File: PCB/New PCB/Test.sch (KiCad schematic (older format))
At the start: 32 parts, among them IC1 REG1117, P1 CONN_2, P2 BATT_CONN, SW1 SWITCH_INV, X1 20 MHz

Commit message: update of new pcb and power supply design
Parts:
- removed ACCELEROMETER1: AIS328DQ, ~, symbol AIS328DQ
- removed C1, C2, C8: C, ~, symbol C
- removed C10, C11: DNI, ~, symbol C
- removed C12: 1uF, ~, symbol C
- removed C13, C3, C6, C7: 0.1 uF, ~, symbol C
- removed C4: 10 nF, ~, symbol C
- removed C5: 470 nF, ~, symbol C
- removed C9: C1 nF, ~, symbol C
- removed CURRENT1: ACS716, symbol ACS716
- removed GYROSCOPE1: A3G4250D, ~, symbol A3G4250D
- removed IC1: REG1117, symbol REG1117
- removed JP1: MOT_ENC, symbol MOT_ENC
- removed JP2: JP, symbol JP
- removed JP3: M05X2PTH, symbol M05X2PTH
- removed JP4: M013X2PTH, symbol M013X2PTH
- removed MOTOR1: LS7366RDIP, symbol LS7366RDIP
- removed P1: CONN_2, symbol CONN_2
- removed P2: BATT_CONN, symbol CONN_2
- removed R1: R, ~, symbol R
- removed R2: 10K, ~, symbol R
- removed R3, R4: DNI, ~, symbol R
- removed R5: 330, ~, symbol R
- removed SW1: SWITCH_INV, ~, symbol SWITCH_INV
- removed X1: 20 MHz, ~, symbol QUARTZCMS4
- added U?: DSPIC33EP512MC806, ~, symbol DSPIC33EP512MC806
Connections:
- net labels removed: +5V, DFLAG, DIO1, DIO2, FAULT_EN, INT1, INT2, INT_1, INT_2, LFLAG, SPI_CLK, SPI_DIN, SPI_DOUT, SPI_SS, VIOUT
- wire segments 166 -> 9
- no-connect marks 36 -> 16
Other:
- note added: "Sensors"
- note added: "XBee Chip"
- moved on the sheet: XBEE1

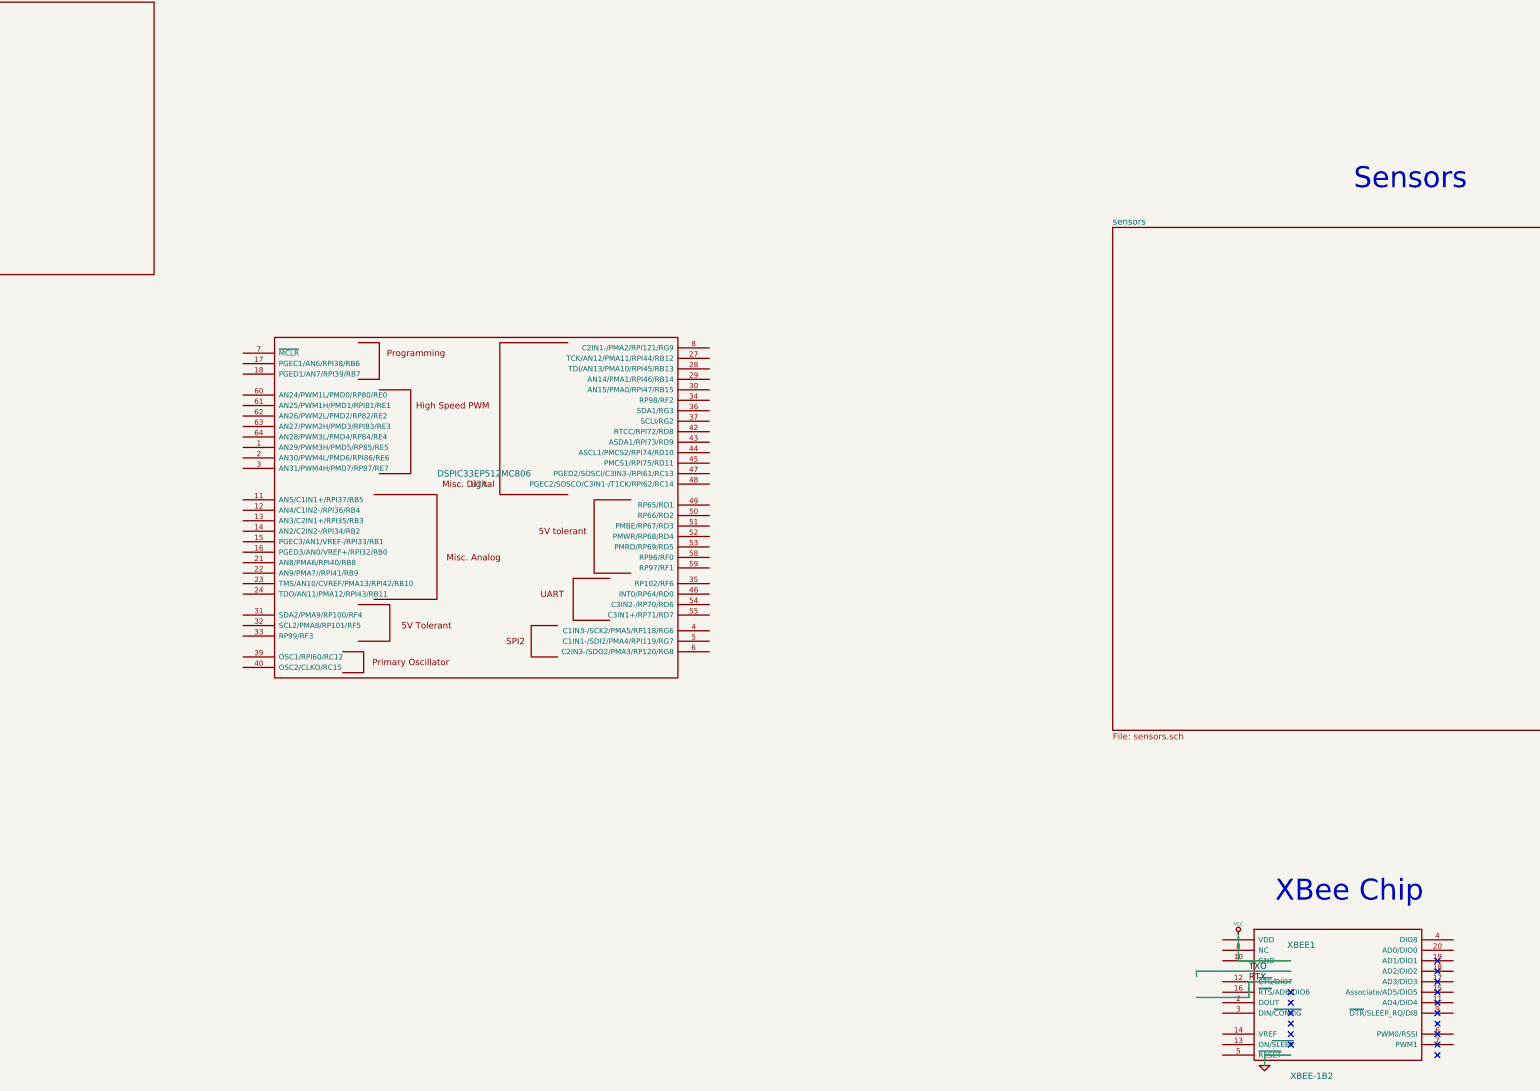
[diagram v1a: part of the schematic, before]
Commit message: Updating Schematic for New PCB
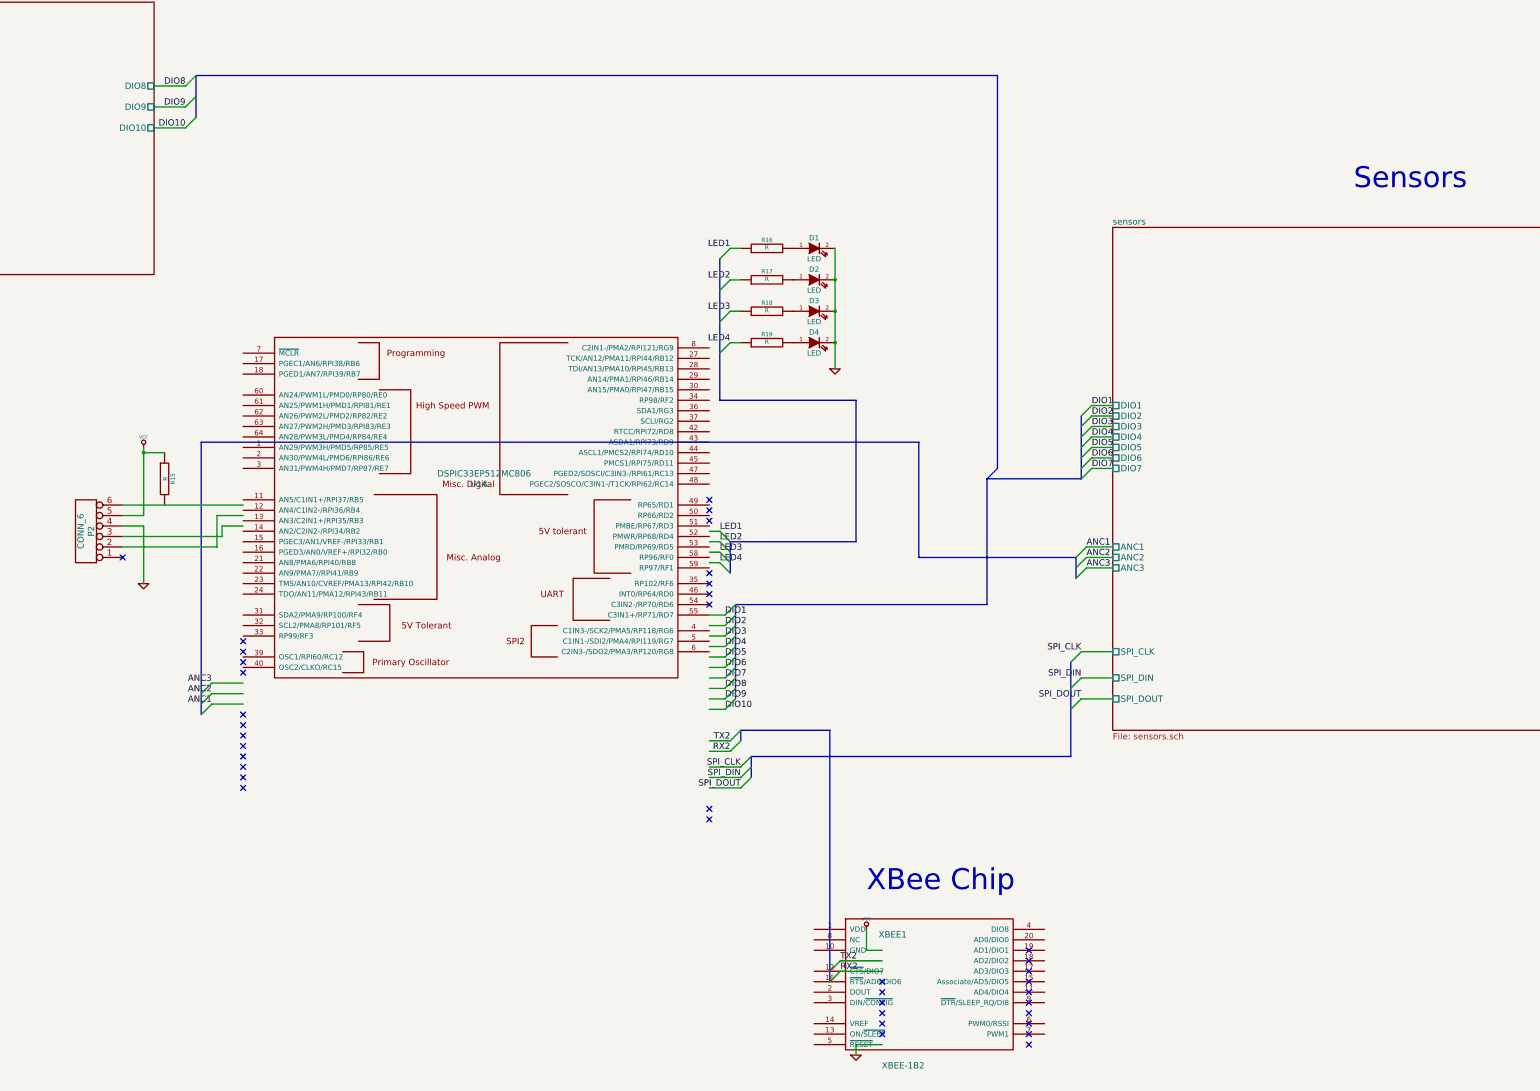
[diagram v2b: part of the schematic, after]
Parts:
- added D1, D2, D3, D4: LED, ~, symbol LED
- added P2: CONN_6, symbol CONN_6
- added R15, R16, R17, R18, R19: R, ~, symbol R
- gave numbers to parts that had none: 1
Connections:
- net labels added: ANC1, ANC2, ANC3, DIO1, DIO10, DIO2, DIO3, DIO4, DIO5, DIO6, DIO7, DIO8, DIO9, LED1, LED2, LED3, LED4, RX2, SPI_CLK, SPI_DIN, SPI_DOUT, TX2
- net labels removed: RTX, TXO
- wire segments 9 -> 61
- no-connect marks 16 -> 38
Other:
- moved on the sheet: XBEE1

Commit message: updated schematic
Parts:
- removed P2: CONN_6, symbol CONN_6
- added CR?: CER_RES, symbol CER_RES
- added JP? (x2): MOT_ENC, symbol MOT_ENC
- added P?: PROG_H, symbol PROG_H
- R15: value R -> 10K
- R16, R17, R18, R19: value R -> 1K
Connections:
- net labels added: +5V, ENC1, ENC2, ENC3, ENC4, ENC5, ENC6
- wire segments 61 -> 69
- no-connect marks 38 -> 29
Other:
- note added: "Power"
- moved on the sheet: D1, D2, D3, D4, R15, R16, R17, R18, R19, U1A, XBEE1

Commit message: more updates
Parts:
- added P?: CONN_2, symbol CONN_2
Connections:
- net labels added: CTS, MagnetControl1, MagnetControl2, MagnetControl[1:2], MotorOut[1:3], Motor_Control[1:6], PWM1H, PWM1L, PWM2H, PWM2L, PWM3H, PWM3L, RTS, RX, SPI_BUS[1:3], TX
- wire segments 69 -> 73
- no-connect marks 29 -> 25
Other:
- note added: "Reset Switch"
- moved on the sheet: XBEE1

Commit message: updated schematic
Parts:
- added D5: LED, ~, symbol LED
- added R2: 1K, ~, symbol R
- added R32: 1M, symbol R
- gave numbers to parts that had none: 5
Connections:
- net labels added: ACCEL1, ACCEL2, ACCEL3, ACCEL[1:3], ANC[1:3], ENCODER1, ENCODER2, ENCODER3, ENCODER4, ENCODER5, ENCODER6, ENC[1:3], GYRO1, GYRO2, GYRO3, GYRO[1:3], LED5, MotorOut[0:2]
- net labels removed: DIO1, DIO10, DIO2, DIO3, DIO4, DIO5, DIO6, DIO7, DIO8, DIO9, ENC4, ENC5, ENC6, MotorOut[1:3]
- wire segments 73 -> 63
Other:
- note added: "NOTE: Global VCC = +3.3V"
- note added: "Need to add the motor hall effect sensors"
- moved on the sheet: D1, D2, D3, D4, R16, R17, R18, R19

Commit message: added notes to schematic
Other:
- note added: "3 on each end of board"
- note added: "6 IR LEDs for Vision group"
- note added: "Add LED"
- note added: "Add decoupling"
- note added: "Change Labels"
- note added: "Mounting Holes as well"
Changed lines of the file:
@@
-EESchema Schematic File Version 2
+EESchema Schematic File Version 2  date 6/2/2013 3:28:30 PM
 LIBS:power
 LIBS:device
@@
 Text Notes 6200 9450 0    60   ~ 0
 Need to add the motor hall effect sensors
+Text Notes 12000 12550 0    60   ~ 0
+Add LED
+Text Notes 8150 13200 0    60   ~ 0
+Change Labels
+Text Notes 10300 14550 0    60   ~ 0
+Add decoupling
+Text Notes 4700 1850 0    157  ~ 0
+6 IR LEDs for Vision group
+Text Notes 5750 2150 0    60   ~ 0
+3 on each end of board
+Text Notes 15500 1750 0    157  ~ 0
+Mounting Holes as well
 $EndSCHEMATC

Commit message: updated schematic and netlist, added flyback diodes
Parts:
- added C53: 0.1uF, symbol C
- added D9: LED, symbol LED
- added P10, P11, P6, P7, P8, P9: CONN_2, symbol CONN_2
- added P12, P13, P14, P15: CONN_1, symbol CONN_1
- added P16: CONN_6, symbol CONN_6
- added R38, R39, R40, R41, R42, R43: 330, symbol R
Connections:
- net labels added: ACCEL0, ACCEL[0..2], ANC0, ANC[0..2], ENC0, ENC[0..2], GYRO0, GYRO[0..2], MagnetControl0, MagnetControl[0..1], MotorControl0, MotorControl1, MotorControl2, MotorControl3, MotorControl4, MotorControl5, MotorControl[0..5], MotorOut[0..2], SPI_BUS0, SPI_BUS1, SPI_BUS2, SPI_BUS[0..2]
- net labels removed: ACCEL3, ACCEL[1:3], ANC3, ANC[1:3], ENC3, ENC[1:3], GYRO3, GYRO[1:3], MagnetControl2, MagnetControl[1:2], MotorOut[0:2], Motor_Control[1:6], PWM1H, PWM1L, PWM2H, PWM2L, PWM3H, PWM3L, RX2, SPI_BUS[1:3], SPI_CLK, SPI_DIN, SPI_DOUT, TX2
- wire segments 63 -> 77
- no-connect marks 25 -> 26
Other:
- note added: "Actuators"
- note added: "Hall effect connector"
- note added: "Mounting Holes"
- note added: "Programming header"
- note added: "Status LED"
- note removed: "Add LED"
- note removed: "Change Labels"
- note removed: "Mounting Holes as well"
- note removed: "Need to add the motor hall effect sensors"

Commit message: order has been placed and confirmed, receipt in project folder
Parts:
- removed CR1: CER_RES, symbol CER_RES
- added CR1: CERAMIC_RES, symbol CERAMIC_RES
- added P17, P18: CONN_1, symbol CONN_1
- added P19: CONN_2, symbol CONN_2
- added R44, R45, R46, R47, R48, R49, R50, R51, R52: 2.2K, ~, symbol R
- added R53: R, ~, symbol R
- added R54: 1K, ~, symbol R
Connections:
- wire segments 77 -> 87
- no-connect marks 26 -> 27
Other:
- note added: "Could be an issue with 5V inputs\nsince 5V powers up first. If PIC is not\non (no 3.3V supply) and 5V pins are driven,\nthere could be a problem."
- note added: "Should have test points for each voltage"
- moved on the sheet: D9, JP1, JP2, P16, R32
